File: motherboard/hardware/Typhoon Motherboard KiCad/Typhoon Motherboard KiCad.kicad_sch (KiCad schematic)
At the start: 6 parts, among them J1 Conn_01x01_Pin, J2 Conn_01x01_Pin, P1 USB_C_Plug_USB2.0, U1 ESP32-S3-WROOM-1

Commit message: Minor Changes
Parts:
- removed J1, J2: Conn_01x01_Pin, symbol Connector:Conn_01x01_Pin
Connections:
- net GND: now also P1.A5 (CC), P1.B5 (VCONN), P1.S1 (SHIELD)
- net +5V: now reaches P1.A4 (VBUS), P1.A9 (VBUS), P1.B4 (VBUS), P1.B9 (VBUS)
- net +3V3: now reaches U1.2 (3V3)
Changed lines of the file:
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@@
 	(generator_version "8.0")
 	(paper "A4")
+	(junction
+		(at 113.03 71.12)
+		(diameter 0)
+		(color 0 0 0 0)
+	)
 	(wire
 		(pts
-			(xy 147.32 55.88) (xy 147.32 64.77)
+			(xy 113.03 71.12) (xy 113.03 73.66)
 		)
 		(stroke
@@
 	(wire
 		(pts
-			(xy 113.03 53.34) (xy 113.03 66.04)
+			(xy 115.57 71.12) (xy 113.03 71.12)
 		)
 		(stroke
@@
 		(pts
 			(xy 121.92 80.01) (xy 113.03 80.01)
+		)
+		(stroke
+			(width 0)
+			(type default)
+		)
+	)
+	(wire
+		(pts
+			(xy 113.03 53.34) (xy 113.03 66.04)
 		)
 		(stroke
@@
 	)
 	(symbol
-		(lib_id "Connector:Conn_01x01_Pin")
-		(at 107.95 53.34 0)
-		(unit 1)
-		(exclude_from_sim no)
-		(in_bom yes)
-		(on_board yes)
-		(dnp no)
-		(fields_autoplaced yes)
-		(property "Reference" "J2"
-			(at 108.585 48.26 0)
-			(effects
-				(font
-					(size 1.27 1.27)
-				)
-			)
-		)
-		(property "Value" "Conn_01x01_Pin"
-			(at 108.585 50.8 0)
-			(effects
-				(font
-					(size 1.27 1.27)
-				)
-			)
-		)
-		(property "Footprint" ""
-			(at 107.95 53.34 0)
-			(effects
-				(font
-					(size 1.27 1.27)
-				)
-				(hide yes)
-			)
-		)
-		(property "Datasheet" "~"
-			(at 107.95 53.34 0)
-			(effects
-				(font
-					(size 1.27 1.27)
-				)
-				(hide yes)
-			)
-		)
-		(property "Description" "Generic connector, single row, 01x01, script generated"
-			(at 107.95 53.34 0)
-			(effects
-				(font
-					(size 1.27 1.27)
-				)
-				(hide yes)
-			)
-		)
-		(pin "1"
-		)
-		(instances
-			(project "Typhoon Motherboard KiCad"
-				(path "/13012fcd-02e9-4b82-8301-52da00f60a6e"
-					(reference "J2")
-					(unit 1)
-				)
-			)
-		)
-	)
-	(symbol
 		(lib_id "Device:R_US")
 		(at 125.73 80.01 90)
@@
 	(symbol
 		(lib_id "power:GND")
+		(at 115.57 71.12 0)
+		(unit 1)
+		(exclude_from_sim no)
+		(in_bom yes)
+		(on_board yes)
+		(dnp no)
+		(fields_autoplaced yes)
+		(property "Reference" "#PWR01"
+			(at 115.57 77.47 0)
+			(effects
+				(font
+					(size 1.27 1.27)
+				)
+				(hide yes)
+			)
+		)
+		(property "Value" "GND"
+			(at 115.57 76.2 0)
+			(effects
+				(font
+					(size 1.27 1.27)
+				)
+			)
+		)
+		(property "Footprint" ""
+			(at 115.57 71.12 0)
+			(effects
+				(font
+					(size 1.27 1.27)
+				)
+				(hide yes)
+			)
+		)
+		(property "Datasheet" ""
+			(at 115.57 71.12 0)
+			(effects
+				(font
+					(size 1.27 1.27)
+				)
+				(hide yes)
+			)
+		)
+		(property "Description" "Power symbol creates a global label with name \"GND\" , ground"
+			(at 115.57 71.12 0)
+			(effects
+				(font
+					(size 1.27 1.27)
+				)
+				(hide yes)
+			)
+		)
+		(pin "1"
+		)
+		(instances
+			(project "Typhoon Motherboard KiCad"
+				(path "/13012fcd-02e9-4b82-8301-52da00f60a6e"
+					(reference "#PWR01")
+					(unit 1)
+				)
+			)
+		)
+	)
+	(symbol
+		(lib_id "power:GND")
+		(at 90.17 104.14 0)
+		(unit 1)
+		(exclude_from_sim no)
+		(in_bom yes)
+		(on_board yes)
+		(dnp no)
+		(fields_autoplaced yes)
+		(property "Reference" "#PWR05"
+			(at 90.17 110.49 0)
+			(effects
+				(font
+					(size 1.27 1.27)
+				)
+				(hide yes)
+			)
+		)
+		(property "Value" "GND"
+			(at 90.17 109.22 0)
+			(effects
+				(font
+					(size 1.27 1.27)
+				)
+			)
+		)
+		(property "Footprint" ""
+			(at 90.17 104.14 0)
+			(effects
+				(font
+					(size 1.27 1.27)
+				)
+				(hide yes)
+			)
+		)
+		(property "Datasheet" ""
+			(at 90.17 104.14 0)
+			(effects
+				(font
+					(size 1.27 1.27)
+				)
+				(hide yes)
+			)
+		)
+		(property "Description" "Power symbol creates a global label with name \"GND\" , ground"
+			(at 90.17 104.14 0)
+			(effects
+				(font
+					(size 1.27 1.27)
+				)
+				(hide yes)
+			)
+		)
+		(pin "1"
+		)
+		(instances
+			(project "Typhoon Motherboard KiCad"
+				(path "/13012fcd-02e9-4b82-8301-52da00f60a6e"
+					(reference "#PWR05")
+					(unit 1)
+				)
+			)
+		)
+	)
+	(symbol
+		(lib_id "power:GND")
 		(at 97.79 104.14 0)
 		(unit 1)
@@
 	)
 	(symbol
-		(lib_id "Connector:Conn_01x01_Pin")
-		(at 142.24 55.88 0)
+		(lib_id "power:+5V")
+		(at 113.03 53.34 0)
 		(unit 1)
 		(exclude_from_sim no)
@@
 		(dnp no)
 		(fields_autoplaced yes)
-		(property "Reference" "J1"
-			(at 142.875 50.8 0)
-			(effects
-				(font
-					(size 1.27 1.27)
-				)
-			)
-		)
-		(property "Value" "Conn_01x01_Pin"
-			(at 142.875 53.34 0)
+		(property "Reference" "#PWR02"
+			(at 113.03 57.15 0)
+			(effects
+				(font
+					(size 1.27 1.27)
+				)
+				(hide yes)
+			)
+		)
+		(property "Value" "+5V"
+			(at 113.03 48.26 0)
 			(effects
 				(font
@@
 		)
 		(property "Footprint" ""
-			(at 142.24 55.88 0)
-			(effects
-				(font
-					(size 1.27 1.27)
-				)
-				(hide yes)
-			)
-		)
-		(property "Datasheet" "~"
-			(at 142.24 55.88 0)
-			(effects
-				(font
-					(size 1.27 1.27)
-				)
-				(hide yes)
-			)
-		)
-		(property "Description" "Generic connector, single row, 01x01, script generated"
-			(at 142.24 55.88 0)
+			(at 113.03 53.34 0)
+			(effects
+				(font
+					(size 1.27 1.27)
+				)
+				(hide yes)
+			)
+		)
+		(property "Datasheet" ""
+			(at 113.03 53.34 0)
+			(effects
+				(font
+					(size 1.27 1.27)
+				)
+				(hide yes)
+			)
+		)
+		(property "Description" "Power symbol creates a global label with name \"+5V\""
+			(at 113.03 53.34 0)
 			(effects
 				(font
@@
 			(project "Typhoon Motherboard KiCad"
 				(path "/13012fcd-02e9-4b82-8301-52da00f60a6e"
-					(reference "J1")
-					(unit 1)
-				)
+					(reference "#PWR02")
+					(unit 1)
+				)
+			)
+		)
+	)
+	(symbol
+		(lib_id "power:+3V3")
+		(at 147.32 64.77 0)
+		(unit 1)
+		(exclude_from_sim no)
+		(in_bom yes)
+		(on_board yes)
+		(dnp no)
+		(fields_autoplaced yes)
+		(property "Reference" "#PWR06"
+			(at 147.32 68.58 0)
+			(effects
+				(font
+					(size 1.27 1.27)
+				)
+				(hide yes)
+			)
+		)
+		(property "Value" "+3V3"
+			(at 147.32 59.69 0)
+			(effects
+				(font
+					(size 1.27 1.27)
+				)
+			)
+		)
+		(property "Footprint" ""
+			(at 147.32 64.77 0)
+			(effects
+				(font
+					(size 1.27 1.27)
+				)
+				(hide yes)
+			)
+		)
+		(property "Datasheet" ""
+			(at 147.32 64.77 0)
+			(effects
+				(font
+					(size 1.27 1.27)
+				)
+				(hide yes)
+			)
+		)
+		(property "Description" "Power symbol creates a global label with name \"+3V3\""
+			(at 147.32 64.77 0)
+			(effects
+				(font
+					(size 1.27 1.27)
+				)
+				(hide yes)
+			)
+		)
+		(pin "1"
+		)
+		(instances
+			(project "Typhoon Motherboard KiCad"
+				(path "/13012fcd-02e9-4b82-8301-52da00f60a6e"
+					(reference "#PWR06")
+					(unit 1)
+				)

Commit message: added v reg
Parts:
- added C1, C2: 22u, Capacitor_SMD:C_0603_1608Metric, symbol Device:C
- added U2: AZ1117-3.3, Package_TO_SOT_SMD:SOT-223-3_TabPin2, symbol Regulator_Linear:AZ1117-3.3
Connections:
- net +5V: now also C1.2, U2.3 (VI)
- net GND: now also C1.1, C2.1, U2.1 (GND)
- new net +3.3V: C2.2, U2.2 (VO)

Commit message: added header
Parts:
- added J1: Conn_01x04_Pin, symbol Connector:Conn_01x04_Pin
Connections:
- net +3V3: now also J1.1 (Pin_1)
- net GND: now also J1.2 (Pin_2)
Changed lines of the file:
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@@
+		)
+	)
+	(wire
+		(pts
+			(xy 186.69 76.2) (xy 181.61 76.2)
+		)
+		(stroke
+			(width 0)
+			(type default)
+		)
+	)
+	(wire
+		(pts
+			(xy 186.69 78.74) (xy 181.61 78.74)
+		)
+		(stroke
+			(width 0)
+			(type default)
 		)
 	)
@@
 	)
 	(symbol
+		(lib_id "power:+3V3")
+		(at 186.69 76.2 0)
+		(unit 1)
+		(exclude_from_sim no)
+		(in_bom yes)
+		(on_board yes)
+		(dnp no)
+		(fields_autoplaced yes)
+		(property "Reference" "#PWR012"
+			(at 186.69 80.01 0)
+			(effects
+				(font
+					(size 1.27 1.27)
+				)
+				(hide yes)
+			)
+		)
+		(property "Value" "+3V3"
+			(at 186.69 71.12 0)
+			(effects
+				(font
+					(size 1.27 1.27)
+				)
+			)
+		)
+		(property "Footprint" ""
+			(at 186.69 76.2 0)
+			(effects
+				(font
+					(size 1.27 1.27)
+				)
+				(hide yes)
+			)
+		)
+		(property "Datasheet" ""
+			(at 186.69 76.2 0)
+			(effects
+				(font
+					(size 1.27 1.27)
+				)
+				(hide yes)
+			)
+		)
+		(property "Description" "Power symbol creates a global label with name \"+3V3\""
+			(at 186.69 76.2 0)
+			(effects
+				(font
+					(size 1.27 1.27)
+				)
+				(hide yes)
+			)
+		)
+		(pin "1"
+		)
+		(instances
+			(project "Typhoon Motherboard KiCad"
+				(path "/13012fcd-02e9-4b82-8301-52da00f60a6e"
+					(reference "#PWR012")
+					(unit 1)
+				)
+			)
+		)
+	)
+	(symbol
 		(lib_id "Regulator_Linear:AZ1117-3.3")
 		(at 60.96 73.66 0)
@@
 					(unit 1)
 				)
+			)
+		)
+	)
+	(symbol
+		(lib_id "Connector:Conn_01x04_Pin")
+		(at 176.53 78.74 0)
+		(unit 1)
+		(exclude_from_sim no)
+		(in_bom yes)
+		(on_board yes)
+		(dnp no)
+		(fields_autoplaced yes)
+		(property "Reference" "J1"
+			(at 177.165 71.12 0)
+			(effects
+				(font
+					(size 1.27 1.27)
+				)
+			)
+		)
+		(property "Value" "Conn_01x04_Pin"
+			(at 177.165 73.66 0)
+			(effects
+				(font
+					(size 1.27 1.27)
+				)
+			)
+		)
+		(property "Footprint" ""
+			(at 176.53 78.74 0)
+			(effects
+				(font
+					(size 1.27 1.27)
+				)
+				(hide yes)
+			)
+		)
+		(property "Datasheet" "~"
+			(at 176.53 78.74 0)
+			(effects
+				(font
+					(size 1.27 1.27)
+				)
+				(hide yes)
+			)
+		)
+		(property "Description" "Generic connector, single row, 01x04, script generated"
+			(at 176.53 78.74 0)
+			(effects
+				(font
+					(size 1.27 1.27)
+				)
+				(hide yes)
+			)
+		)
+		(pin "4"
+		)
+		(pin "2"
+		)
+		(pin "1"
+		)
+		(pin "3"
+		)
+		(instances
+			(project "Typhoon Motherboard KiCad"
+				(path "/13012fcd-02e9-4b82-8301-52da00f60a6e"
+					(reference "J1")
+					(unit 1)
+				)
+			)
+		)
+	)
+	(symbol
+		(lib_id "power:GND")
+		(at 186.69 78.74 0)
+		(unit 1)
+		(exclude_from_sim no)
+		(in_bom yes)
+		(on_board yes)
+		(dnp no)
+		(fields_autoplaced yes)
+		(property "Reference" "#PWR013"
+			(at 186.69 85.09 0)
+			(effects
+				(font
+					(size 1.27 1.27)
+				)
+				(hide yes)
+			)
+		)
+		(property "Value" "GND"
+			(at 186.69 83.82 0)
+			(effects
+				(font
+					(size 1.27 1.27)
+				)
+			)
+		)
+		(property "Footprint" ""
+			(at 186.69 78.74 0)
+			(effects
+				(font
+					(size 1.27 1.27)
+				)
+				(hide yes)
+			)
+		)
+		(property "Datasheet" ""
+			(at 186.69 78.74 0)
+			(effects
+				(font
+					(size 1.27 1.27)
+				)
+				(hide yes)
+			)
+		)
+		(property "Description" "Power symbol creates a global label with name \"GND\" , ground"
+			(at 186.69 78.74 0)
+			(effects
+				(font
+					(size 1.27 1.27)
+				)
+				(hide yes)
+			)
+		)
+		(pin "1"
+		)
+		(instances
+			(project "Typhoon Motherboard KiCad"
+				(path "/13012fcd-02e9-4b82-8301-52da00f60a6e"
+					(reference "#PWR013")
+					(unit 1)
+				)

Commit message: Update Typhoon Motherboard KiCad.kicad_sch
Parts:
- J1: footprint (none) -> Connector_PinHeader_2.00mm:PinHeader_1x04_P2.00mm_Vertical
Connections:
- net SDA: now reaches J1.3 (Pin_3)
- net SCL: now reaches J1.4 (Pin_4)
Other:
- moved on the sheet: C1, C2, J1, U2

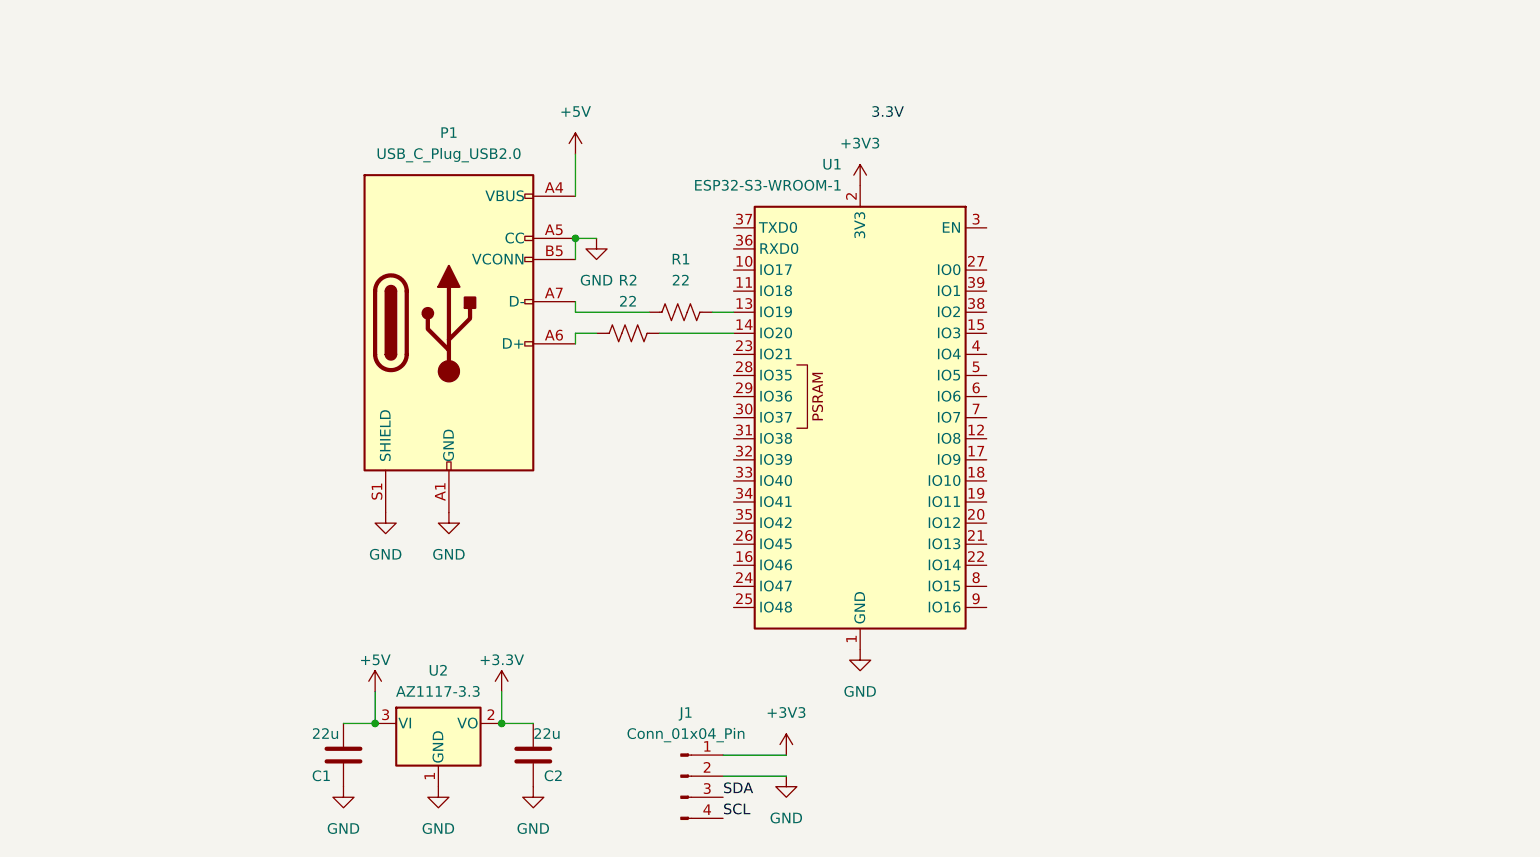
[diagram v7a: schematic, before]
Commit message: added new symbol for TJA1051
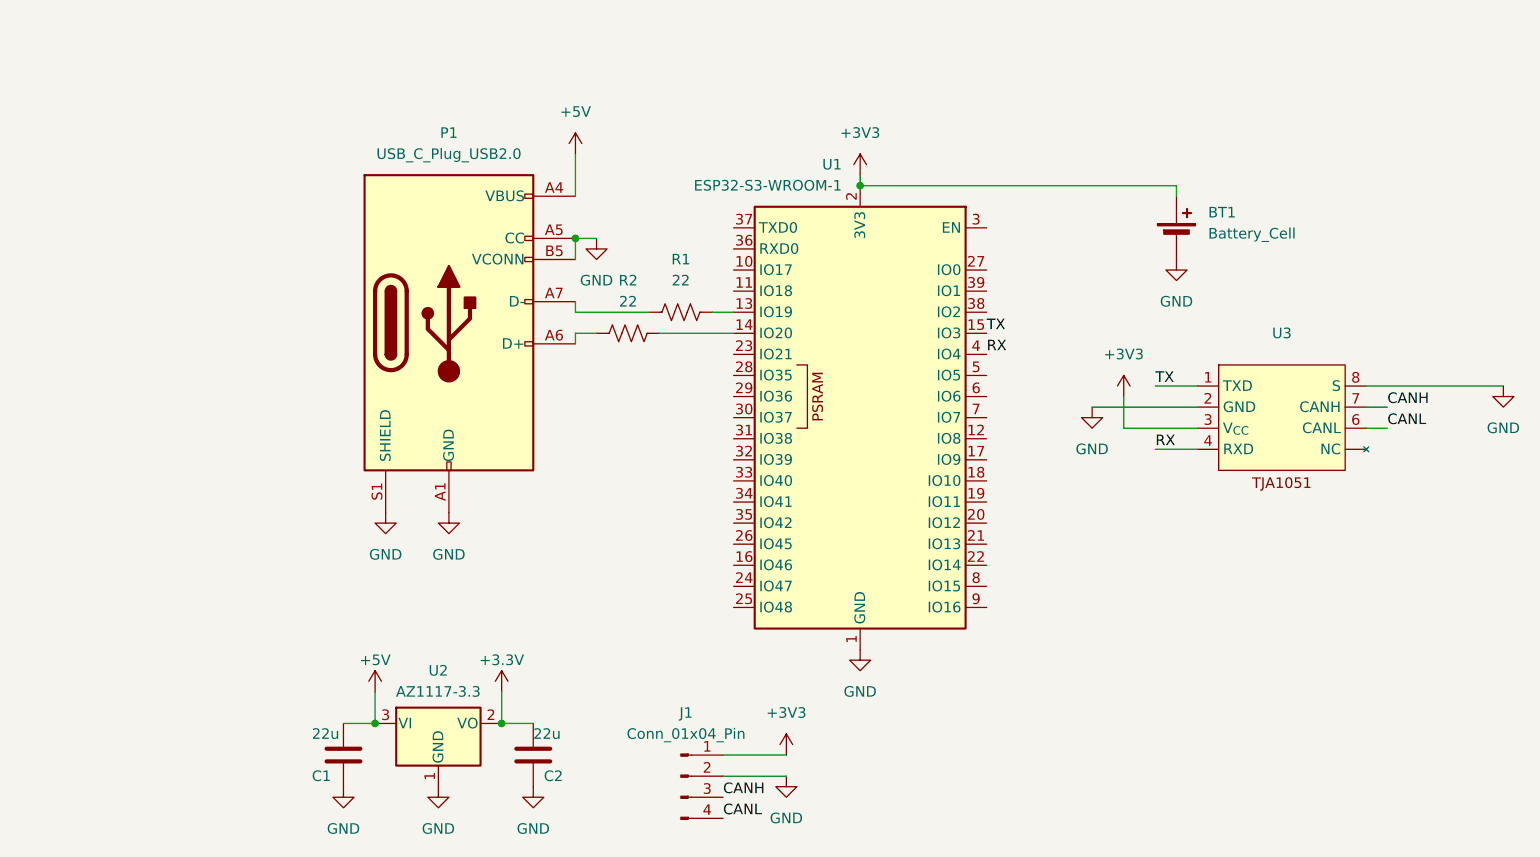
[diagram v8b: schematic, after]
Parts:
- added BT1: Battery_Cell, Battery:BatteryHolder_Keystone_3009_1x2450, symbol Device:Battery_Cell
- added U3: ~, symbol Interface_CAN_LIN:TJA1051
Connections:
- net +3V3: now also BT1.1 (+), U3.3 (V_{CC})
- net GND: now also BT1.2 (-), U3.2 (GND), U3.8 (S)
- net TX: now reaches U1.15 (IO3)
- net TX: now also U3.1 (TXD)
- net RX: now reaches U1.4 (IO4)
- net RX: now also U3.4 (RXD)
- net SCL renamed CANL
- net CANL: now also U3.6 (CANL)
- net SDA renamed CANH
- net CANH: now also U3.7 (CANH)
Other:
- note removed: "3.3V"
